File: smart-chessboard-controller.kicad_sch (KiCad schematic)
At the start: 59 parts, among them J101 USB_C_Receptacle_USB2.0, J103 Micro_SD_Card_Det_Hirose_DM3C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, J104 Conn_02x03_Odd_Even, J105 NX3224T024, Q101 S8050, Q102 S8050, SW104 SW_SPST, SW106 SW_SPST, SW107 SW_SPST, SW109 SW_SPST, U101 XC6220B331MR-G, U102 ESP32-WROOM-32E (8MB), U103 SP0503BAHT, U104 PCA9548APW, U105 CP2102-GMR

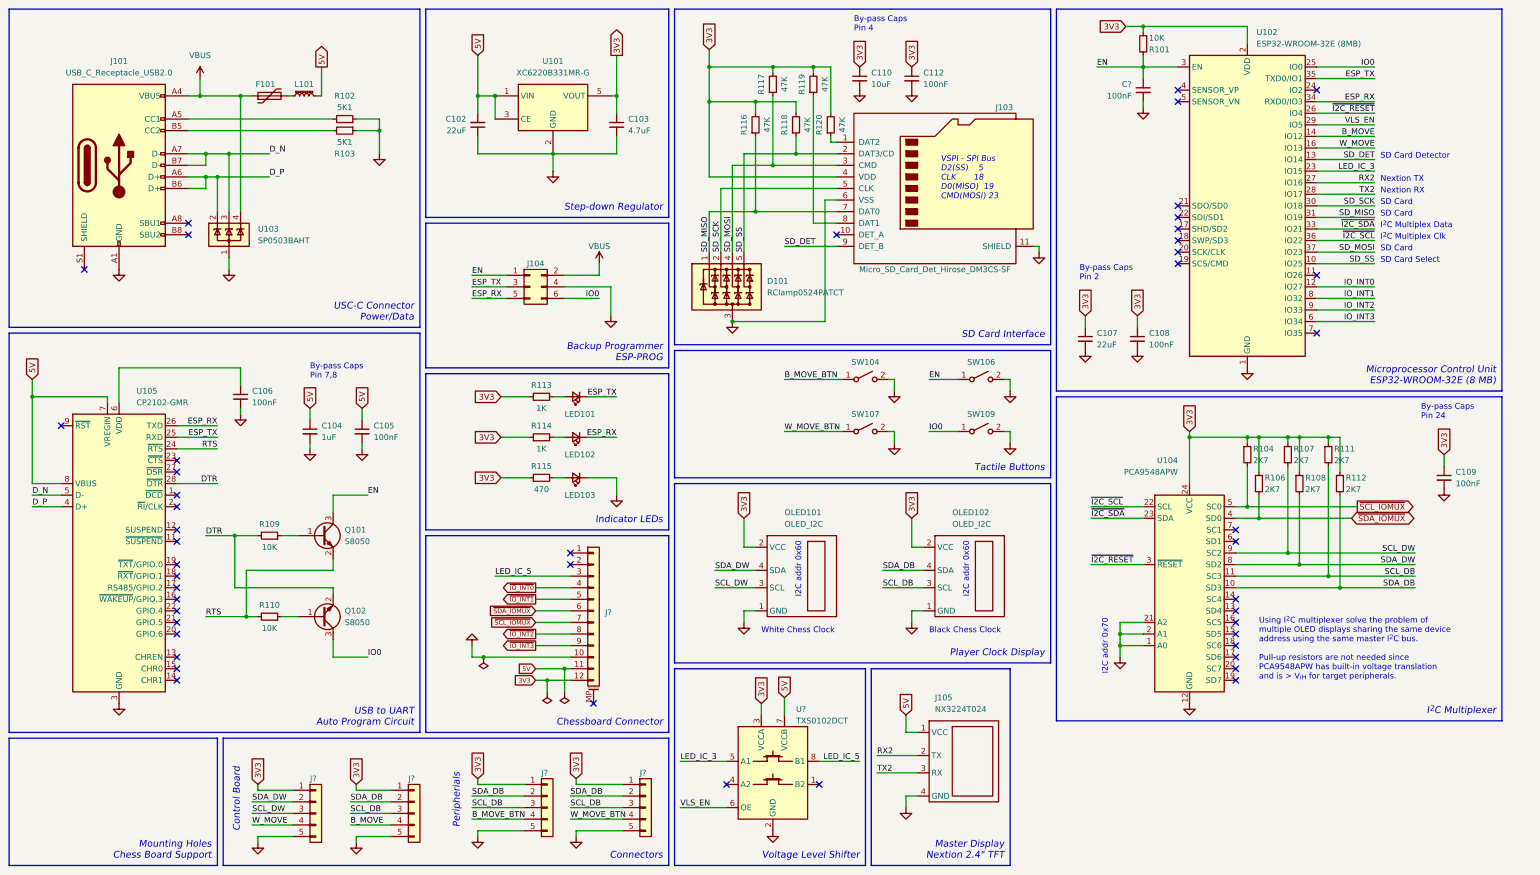
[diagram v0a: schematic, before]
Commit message: move around pins on ESP32 to optimize PCB layout
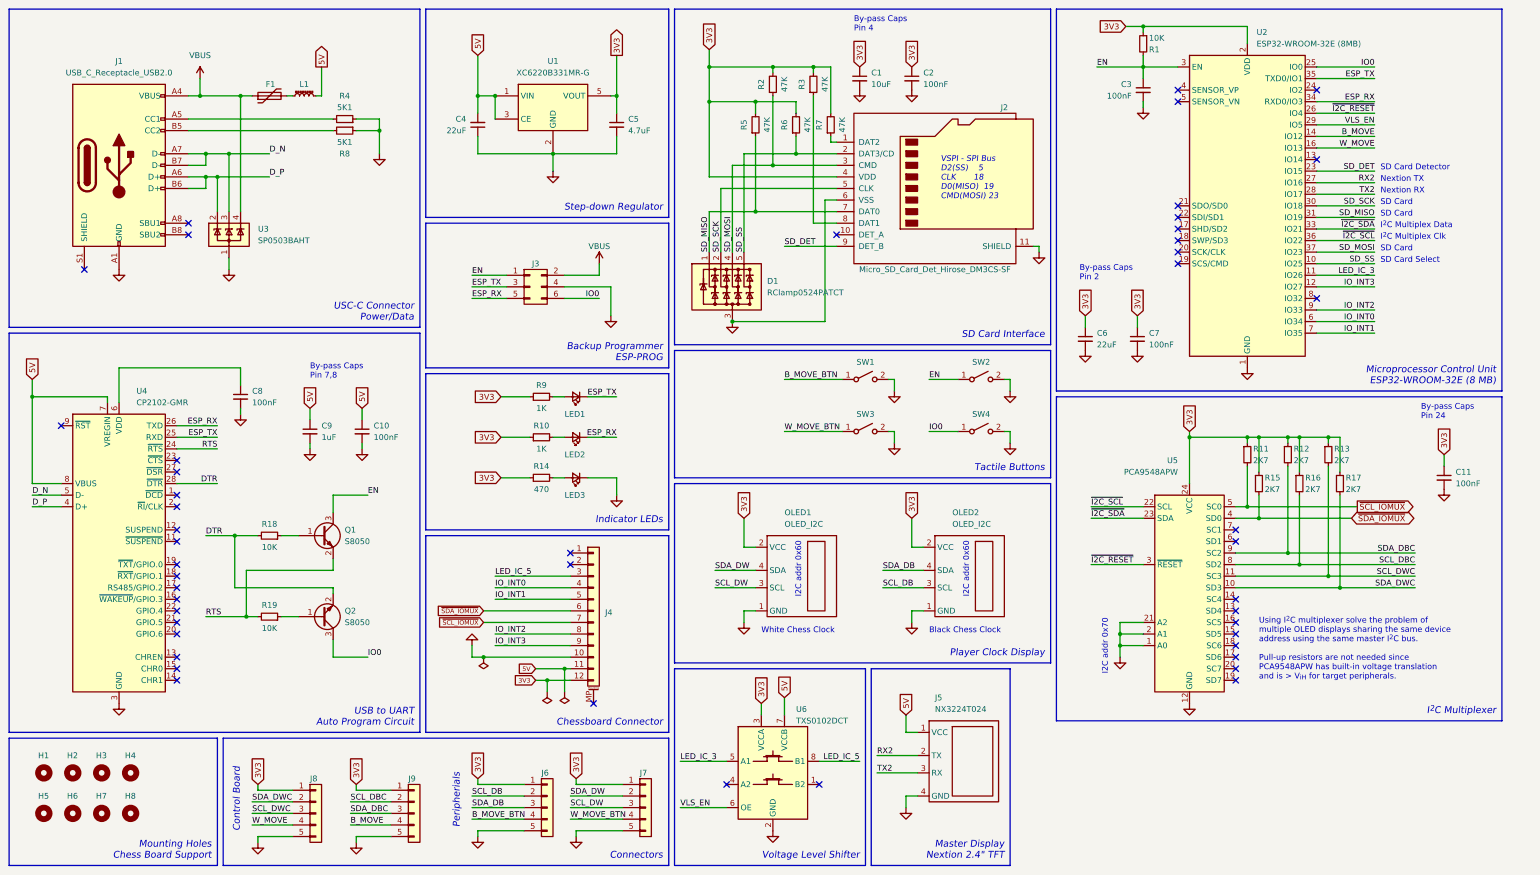
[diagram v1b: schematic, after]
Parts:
- added H1, H2, H3, H4, H5, H6, H7, H8: MountingHole, MountingHole:MountingHole_3.2mm_M3_Pad_TopBottom, symbol Mechanical:MountingHole
- J5: renamed from J105; footprint User Custom Footprint:NX3224T024 -> Connector_JST:JST_PH_S4B-PH-K_1x04_P2.00mm_Horizontal; LCSC (none) -> C157926
- J6, J7, J8, J9: renamed from J?; LCSC (none) -> C157923
- gave numbers to parts that had none: 3
- renumbered C110 to C1, C105 to C10, C109 to C11, C112 to C2, C102 to C4, C103 to C5, C107 to C6, C108 to C7, C106 to C8, C104 to C9, D101 to D1, F101 to F1, J101 to J1, J103 to J2, J104 to J3, L101 to L1, LED101 to LED1, LED102 to LED2, LED103 to LED3, OLED101 to OLED1, OLED102 to OLED2, Q101 to Q1, Q102 to Q2, R101 to R1, R114 to R10, R104 to R11, R107 to R12, R111 to R13, R115 to R14, R106 to R15, R108 to R16, R112 to R17, R109 to R18, R110 to R19, R117 to R2, R119 to R3, R102 to R4, R116 to R5, R118 to R6, R120 to R7, R103 to R8, R113 to R9, SW104 to SW1, SW106 to SW2, SW107 to SW3, SW109 to SW4, U101 to U1, U102 to U2, U103 to U3, U105 to U4, U104 to U5
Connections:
- net ~{IO_INT0} is gone; now on net IO_INT0: J4.4 (Pin_4)
- net ~{IO_INT1} is gone; now on net IO_INT1: J4.5 (Pin_5)
- net ~{IO_INT2} is gone; now on net IO_INT2: J4.8 (Pin_8)
- net ~{IO_INT3} is gone; now on net IO_INT3: J4.9 (Pin_9)
- net IO_INT0: now also U2.6 (IO34); no longer U2.12 (IO27)
- net IO_INT1: now also U2.7 (IO35); no longer U2.8 (IO32)
- net IO_INT3: now also U2.12 (IO27); no longer U2.6 (IO34)
- net LED_IC_3: now also U2.11 (IO26); no longer U2.23 (IO15)
- net SCL_DB: now also J6.2 (Pin_2); no longer J6.3 (Pin_3), J7.3 (Pin_3), J9.3 (Pin_3), R13.2, U5.11 (SC3)
- net SCL_DW: now also J7.3 (Pin_3); no longer J8.3 (Pin_3), R12.2, U5.9 (SC2)
- net SDA_DB: now also J6.3 (Pin_3); no longer J6.2 (Pin_2), J7.2 (Pin_2), J9.2 (Pin_2), R17.2, U5.10 (SD3)
- net SDA_DW: now also J7.2 (Pin_2); no longer J8.2 (Pin_2), R16.2, U5.8 (SD2)
- net SD_DET: now also U2.23 (IO15); no longer U2.13 (IO14)
- new net SCL_DBC: J9.2 (Pin_2), R16.2, U5.8 (SD2)
- new net SCL_DWC: J8.3 (Pin_3), R13.2, U5.11 (SC3)
- new net SDA_DBC: J9.3 (Pin_3), R12.2, U5.9 (SC2)
- new net SDA_DWC: J8.2 (Pin_2), R17.2, U5.10 (SD3)

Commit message: change mounting hole size
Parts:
- H1, H2, H3, H4, H5, H6, H7, H8: footprint MountingHole:MountingHole_3.2mm_M3_Pad_TopBottom -> MountingHole:MountingHole_2.7mm_M2.5_DIN965_Pad_TopBottom
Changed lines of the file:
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@@
       (effects (font (size 1.27 1.27)) (justify left) hide)
     )
-    (property "Footprint" "MountingHole:MountingHole_3.2mm_M3_Pad_TopBottom" (id 2) (at 34.29 190.5 0)
+    (property "Footprint" "MountingHole:MountingHole_2.7mm_M2.5_DIN965_Pad_TopBottom" (id 2) (at 34.29 190.5 0)
       (effects (font (size 1.27 1.27)) hide)
     )
@@
       (effects (font (size 1.27 1.27)) (justify left) hide)
     )
-    (property "Footprint" "MountingHole:MountingHole_3.2mm_M3_Pad_TopBottom" (id 2) (at 34.29 181.61 0)
+    (property "Footprint" "MountingHole:MountingHole_2.7mm_M2.5_DIN965_Pad_TopBottom" (id 2) (at 34.29 181.61 0)
       (effects (font (size 1.27 1.27)) hide)
     )
@@
       (effects (font (size 1.27 1.27)) (justify left) hide)
     )
-    (property "Footprint" "MountingHole:MountingHole_3.2mm_M3_Pad_TopBottom" (id 2) (at 40.64 181.61 0)
+    (property "Footprint" "MountingHole:MountingHole_2.7mm_M2.5_DIN965_Pad_TopBottom" (id 2) (at 40.64 181.61 0)
       (effects (font (size 1.27 1.27)) hide)
     )
@@
       (effects (font (size 1.27 1.27)) (justify left) hide)
     )
-    (property "Footprint" "MountingHole:MountingHole_3.2mm_M3_Pad_TopBottom" (id 2) (at 27.94 181.61 0)
+    (property "Footprint" "MountingHole:MountingHole_2.7mm_M2.5_DIN965_Pad_TopBottom" (id 2) (at 27.94 181.61 0)
       (effects (font (size 1.27 1.27)) hide)
     )
@@
       (effects (font (size 1.27 1.27)) (justify left) hide)
     )
-    (property "Footprint" "MountingHole:MountingHole_3.2mm_M3_Pad_TopBottom" (id 2) (at 40.64 190.5 0)
+    (property "Footprint" "MountingHole:MountingHole_2.7mm_M2.5_DIN965_Pad_TopBottom" (id 2) (at 40.64 190.5 0)
       (effects (font (size 1.27 1.27)) hide)
     )
@@
       (effects (font (size 1.27 1.27)) (justify left) hide)
     )
-    (property "Footprint" "MountingHole:MountingHole_3.2mm_M3_Pad_TopBottom" (id 2) (at 27.94 190.5 0)
+    (property "Footprint" "MountingHole:MountingHole_2.7mm_M2.5_DIN965_Pad_TopBottom" (id 2) (at 27.94 190.5 0)
       (effects (font (size 1.27 1.27)) hide)
     )
@@
       (effects (font (size 1.27 1.27)) (justify left) hide)
     )
-    (property "Footprint" "MountingHole:MountingHole_3.2mm_M3_Pad_TopBottom" (id 2) (at 21.59 190.5 0)
+    (property "Footprint" "MountingHole:MountingHole_2.7mm_M2.5_DIN965_Pad_TopBottom" (id 2) (at 21.59 190.5 0)
       (effects (font (size 1.27 1.27)) hide)
     )
@@
       (effects (font (size 1.27 1.27)) (justify left) hide)
     )
-    (property "Footprint" "MountingHole:MountingHole_3.2mm_M3_Pad_TopBottom" (id 2) (at 21.59 181.61 0)
+    (property "Footprint" "MountingHole:MountingHole_2.7mm_M2.5_DIN965_Pad_TopBottom" (id 2) (at 21.59 181.61 0)
       (effects (font (size 1.27 1.27)) hide)
     )
@@
     )
     (path "/e2d2c486-75b5-4941-a1b1-3194a5bb7a47"
-      (reference "H1") (unit 1) (value "MountingHole") (footprint "MountingHole:MountingHole_3.2mm_M3_Pad_TopBottom")
+      (reference "H1") (unit 1) (value "MountingHole") (footprint "MountingHole:MountingHole_2.7mm_M2.5_DIN965_Pad_TopBottom")
     )
     (path "/87721282-47f1-45eb-a878-3076d3dcd24d"
-      (reference "H2") (unit 1) (value "MountingHole") (footprint "MountingHole:MountingHole_3.2mm_M3_Pad_TopBottom")
+      (reference "H2") (unit 1) (value "MountingHole") (footprint "MountingHole:MountingHole_2.7mm_M2.5_DIN965_Pad_TopBottom")
     )
     (path "/245828a3-f1d1-44f8-a141-68c9c0ffe51d"
-      (reference "H3") (unit 1) (value "MountingHole") (footprint "MountingHole:MountingHole_3.2mm_M3_Pad_TopBottom")
+      (reference "H3") (unit 1) (value "MountingHole") (footprint "MountingHole:MountingHole_2.7mm_M2.5_DIN965_Pad_TopBottom")
     )
     (path "/810ade1d-ffff-47b3-b115-15ff0d742a7a"
-      (reference "H4") (unit 1) (value "MountingHole") (footprint "MountingHole:MountingHole_3.2mm_M3_Pad_TopBottom")
+      (reference "H4") (unit 1) (value "MountingHole") (footprint "MountingHole:MountingHole_2.7mm_M2.5_DIN965_Pad_TopBottom")
     )
     (path "/cec9b599-1f42-4dba-b9c0-95aba3e6bbdc"
-      (reference "H5") (unit 1) (value "MountingHole") (footprint "MountingHole:MountingHole_3.2mm_M3_Pad_TopBottom")
+      (reference "H5") (unit 1) (value "MountingHole") (footprint "MountingHole:MountingHole_2.7mm_M2.5_DIN965_Pad_TopBottom")
     )
     (path "/b49f2854-d875-437a-ae11-768f5a97cd6c"
-      (reference "H6") (unit 1) (value "MountingHole") (footprint "MountingHole:MountingHole_3.2mm_M3_Pad_TopBottom")
+      (reference "H6") (unit 1) (value "MountingHole") (footprint "MountingHole:MountingHole_2.7mm_M2.5_DIN965_Pad_TopBottom")
     )
     (path "/0790086f-6d4f-4758-985b-a46cdfe42c93"
-      (reference "H7") (unit 1) (value "MountingHole") (footprint "MountingHole:MountingHole_3.2mm_M3_Pad_TopBottom")
+      (reference "H7") (unit 1) (value "MountingHole") (footprint "MountingHole:MountingHole_2.7mm_M2.5_DIN965_Pad_TopBottom")
     )
     (path "/abc95e5a-46b8-4c0e-a9ba-e2dcd8cc0ae4"
-      (reference "H8") (unit 1) (value "MountingHole") (footprint "MountingHole:MountingHole_3.2mm_M3_Pad_TopBottom")
+      (reference "H8") (unit 1) (value "MountingHole") (footprint "MountingHole:MountingHole_2.7mm_M2.5_DIN965_Pad_TopBottom")
     )
     (path "/582a69f8-5434-4554-917e-70d2bc28584c"

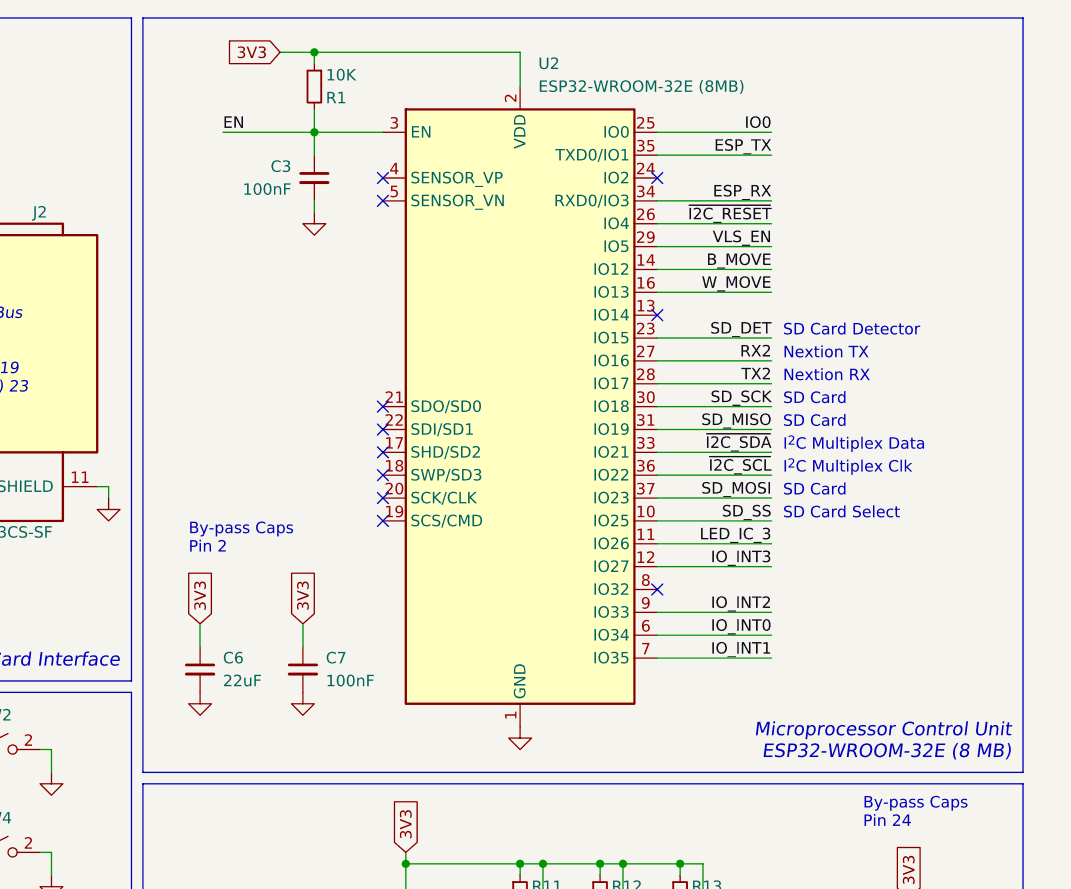
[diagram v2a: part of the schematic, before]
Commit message: add all traces and power traces
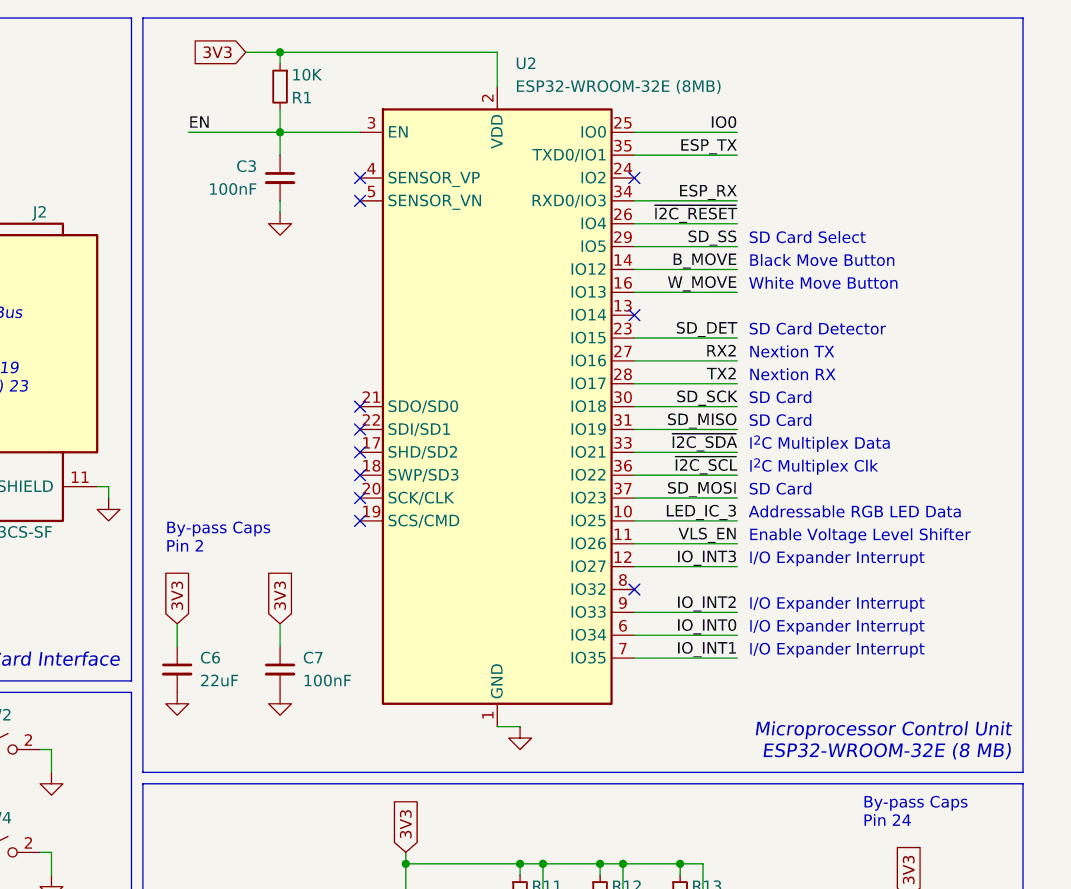
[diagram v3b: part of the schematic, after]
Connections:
- net LED_IC_3: now also U2.10 (IO25); no longer U2.11 (IO26)
- net SD_SS: now also U2.29 (IO5); no longer U2.10 (IO25)
- net VLS_EN: now also U2.11 (IO26); no longer U2.29 (IO5)
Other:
- note added: "Addressable RGB LED Data"
- note added: "Black Move Button"
- note added: "Enable Voltage Level Shifter"
- note added: "I/O Expander Interrupt"
- note added: "White Move Button"
- moved on the sheet: C3, C6, C7, R1, U2

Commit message: update labels
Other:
- note removed: "White Move Button"
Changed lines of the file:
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@@
     (effects (font (size 1.5 1.5) italic) (justify right bottom))
   )
-  (text "White Move Button" (at 311.15 44.45 0)
+  (text "Black Move Button" (at 311.15 44.45 0)
     (effects (font (size 1.27 1.27)) (justify left bottom))
   )
